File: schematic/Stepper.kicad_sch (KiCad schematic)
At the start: 0 parts

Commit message: Create stepper driver schematic
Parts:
- added J6: B5B-XH-A, B5B-XH-A_LF__SN_:JST_B5B-XH-A_LF__SN_, symbol B5B-XH-A_LF__SN_:B5B-XH-A_LF__SN_
- added U4: ULN2003AD, ULN2003AD:SOIC127P600X175-16N, symbol ULN2003AD:ULN2003AD
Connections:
- new net: J6.4, U4.13 (4C)
- new net: J6.3, U4.14 (3C)
- new net: J6.2, U4.15 (2C)
- new net: J6.1, U4.16 (1C)
- new net +5V: J6.5, U4.9 (COM)
- new net GND: U4.5 (5B), U4.6 (6B), U4.7 (7B), U4.8 (E)
- new net STEPPER_A: U4.1 (1B)
- new net STEPPER_B: U4.2 (2B)
- new net STEPPER_C: U4.3 (3B)
- new net STEPPER_D: U4.4 (4B)
- no-connect marks 0 -> 3

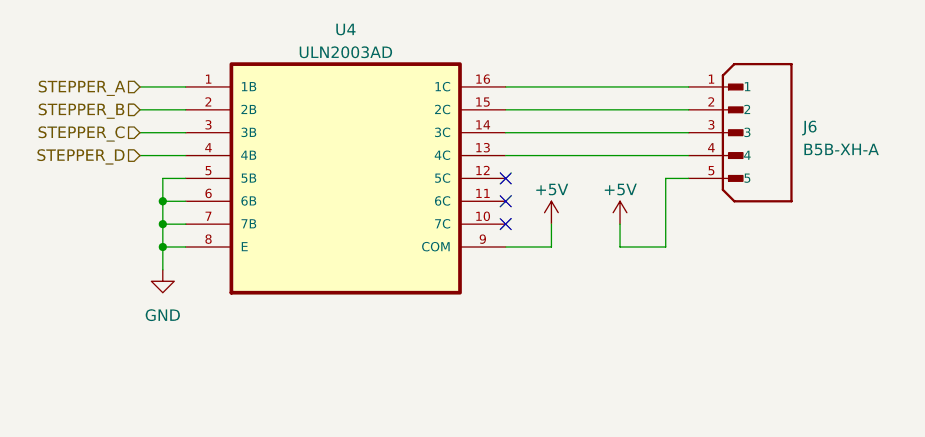
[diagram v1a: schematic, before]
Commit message: Assign footprints
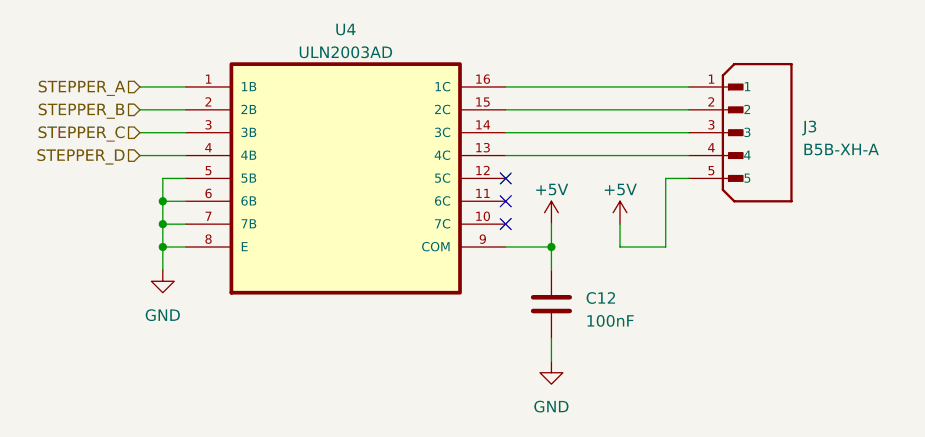
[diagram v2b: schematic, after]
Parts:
- added C12: 100nF, Capacitor_SMD:C_0603_1608Metric, symbol Device:C
- J3: renamed from J6; footprint B5B-XH-A_LF__SN_:JST_B5B-XH-A_LF__SN_ -> Connector:JST_B5B-XH-A_LF__SN_
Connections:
- net +5V: now also C12.1
- net GND: now also C12.2
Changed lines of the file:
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@@
     (rev "v1")
+  )
+  (junction (at 167.64 104.14) (diameter 0) (color 0 0 0 0)
   )
   (junction (at 124.46 101.6) (diameter 0) (color 0 0 0 0)
@@
   (no_connect (at 162.56 99.06))
   (no_connect (at 162.56 101.6))
+  (wire (pts (xy 167.64 104.14) (xy 167.64 106.68))
+    (stroke (width 0) (type default))
+  )
   (wire (pts (xy 121.92 91.44) (xy 127 91.44))
     (stroke (width 0) (type default))
@@
   )
   (wire (pts (xy 127 104.14) (xy 124.46 104.14))
+    (stroke (width 0) (type default))
+  )
+  (wire (pts (xy 167.64 114.3) (xy 167.64 116.84))
     (stroke (width 0) (type default))
   )
@@
         (path "/c978750c-b285-44b2-8d41-37a456977bcd/f4a1c357-f969-4a11-a296-8eff26bf6bb6"
           (reference "#PWR040") (unit 1)
+        )
+      )
+    )
+  )
+  (symbol (lib_id "power:GND") (at 167.64 116.84 0) (unit 1)
+    (in_bom yes) (on_board yes) (dnp no) (fields_autoplaced)
+    (property "Reference" "#PWR041" (at 167.64 123.19 0)
+      (effects (font (size 1.27 1.27)) hide)
+    )
+    (property "Value" "GND" (at 167.64 121.92 0)
+      (effects (font (size 1.27 1.27)))
+    )
+    (property "Footprint" "" (at 167.64 116.84 0)
+      (effects (font (size 1.27 1.27)) hide)
+    )
+    (property "Datasheet" "" (at 167.64 116.84 0)
+      (effects (font (size 1.27 1.27)) hide)
+    )
+    (pin "1")
+    (instances
+      (project "ISSptr"
+        (path "/c978750c-b285-44b2-8d41-37a456977bcd/f4a1c357-f969-4a11-a296-8eff26bf6bb6"
+          (reference "#PWR041") (unit 1)
         )
       )
@@
     )
   )
+  (symbol (lib_id "Device:C") (at 167.64 110.49 0) (unit 1)
+    (in_bom yes) (on_board yes) (dnp no) (fields_autoplaced)
+    (property "Reference" "C12" (at 171.45 109.855 0)
+      (effects (font (size 1.27 1.27)) (justify left))
+    )
+    (property "Value" "100nF" (at 171.45 112.395 0)
+      (effects (font (size 1.27 1.27)) (justify left))
+    )
+    (property "Footprint" "Capacitor_SMD:C_0603_1608Metric" (at 168.6052 114.3 0)
+      (effects (font (size 1.27 1.27)) hide)
+    )
+    (property "Datasheet" "~" (at 167.64 110.49 0)
+      (effects (font (size 1.27 1.27)) hide)
+    )
+    (pin "1")
+    (pin "2")
+    (instances
+      (project "ISSptr"
+        (path "/c978750c-b285-44b2-8d41-37a456977bcd/f4a1c357-f969-4a11-a296-8eff26bf6bb6"
+          (reference "C12") (unit 1)
+        )
+      )
+    )
+  )
   (symbol (lib_id "B5B-XH-A_LF__SN_:B5B-XH-A_LF__SN_") (at 190.5 91.44 0) (unit 1)
     (in_bom yes) (on_board yes) (dnp no) (fields_autoplaced)
-    (property "Reference" "J6" (at 195.58 90.805 0)
+    (property "Reference" "J3" (at 195.58 90.805 0)
       (effects (font (size 1.27 1.27)) (justify left))
     )
@@
       (effects (font (size 1.27 1.27)) (justify left))
     )
-    (property "Footprint" "B5B-XH-A_LF__SN_:JST_B5B-XH-A_LF__SN_" (at 190.5 91.44 0)
+    (property "Footprint" "Connector:JST_B5B-XH-A_LF__SN_" (at 190.5 91.44 0)
       (effects (font (size 1.27 1.27)) (justify bottom) hide)
     )
@@
       (project "ISSptr"
         (path "/c978750c-b285-44b2-8d41-37a456977bcd/f4a1c357-f969-4a11-a296-8eff26bf6bb6"
-          (reference "J6") (unit 1)
-        )
-      )
+          (reference "J3") (unit 1)
+        )
+      )

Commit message: Setup PCB for production
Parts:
- C12: LCSC (none) -> C1591
- J3: LCSC (none) -> C157991
- U4: LCSC (none) -> C908113
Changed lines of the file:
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@@
       (effects (font (size 1.27 1.27)) (justify bottom) hide)
+    )
+    (property "LCSC" "C908113" (at 144.78 96.52 0)
+      (effects (font (size 1.27 1.27)) hide)
     )
     (pin "1")
@@
     )
     (property "Datasheet" "~" (at 167.64 110.49 0)
+      (effects (font (size 1.27 1.27)) hide)
+    )
+    (property "LCSC" "C1591" (at 167.64 110.49 0)
       (effects (font (size 1.27 1.27)) hide)
     )
@@
       (effects (font (size 1.27 1.27)) (justify bottom) hide)
     )
+    (property "LCSC" "C157991" (at 190.5 91.44 0)
+      (effects (font (size 1.27 1.27)) hide)
+    )
     (pin "1")
